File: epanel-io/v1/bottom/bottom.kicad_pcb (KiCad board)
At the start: 2 copper layers, 86.5 x 103 mm, 152 parts, among them J1 Conn_01x05_Male, J2 Screw_Terminal_01x05, J3 Screw_Terminal_01x05, J4 Screw_Terminal_01x05, J5 Screw_Terminal_01x05, J6 Screw_Terminal_01x03, J7 Screw_Terminal_01x03, Q1 IRF830, Q10 IRF830, Q11 IRF830, Q12 IRF830, Q13 IRF830, Q14 IRF830, Q15 IRF830, Q16 IRF830, Q17 IRF830, Q18 IRF830, Q19 IRF830, Q2 IRF830, Q20 IRF830, Q3 IRF830, Q4 IRF830, Q5 IRF830, Q6 IRF830, Q7 IRF830, Q8 IRF830, Q9 IRF830, U1 Pico, U10 4N35, U11 H11AA1, U12 4N35, U13 H11AA1, U14 4N35, U15 H11AA1, U16 4N35, U17 H11AA1, U18 4N35, U19 H11AA1, U2 H11AA1, U20 4N35, U21 H11AA1, U22 4N35, U3 H11AA1, U4 4N35, U5 H11AA1, U6 4N35, U7 H11AA1, U8 4N35, U9 H11AA1

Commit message: bottom board first draft
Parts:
- removed C1, C10, C2, C3, C4, C5, C6, C7, C8, C9: 2.2uF/63V, Capacitor_SMD:C_1206_3216Metric
- removed D1, D11, D13, D15, D17, D19, D3, D5, D7, D9: 10V/0.4W, Diode_SMD:D_SOD-123
- removed D10, D12, D14, D16, D18, D2, D20, D4, D6, D8: 1N4007, Diode_SMD:D_SMA
- removed R1, R11, R18, R25, R32, R39, R4, R46, R53, R60, R67: 10KΩ, Resistor_SMD:R_0603_1608Metric
- removed R10, R12, R13, R16, R17, R19, R2, R20, R23, R24, R26, R27, R3, R30, R31, R33, R34, R37, R38, R40, R41, R44, R45, R47, R48, R5, R51, R52, R54, R55, R58, R59, R6, R61, R62, R65, R66, R68, R69, R72, R73, R9: 33KΩ/0.5W, Resistor_SMD:R_0805_2012Metric
- removed R14, R21, R28, R35, R42, R49, R56, R63, R7, R70: 330Ω, Resistor_SMD:R_0603_1608Metric
- removed R15, R22, R29, R36, R43, R50, R57, R64, R71, R8: 22KΩ, Resistor_SMD:R_0603_1608Metric
- removed U1: Pico, MCU_RaspberryPi_and_Boards:RPi_Pico_SMD_TH
- removed U10, U12, U14, U16, U18, U20, U22, U4, U6, U8: 4N35, Package_DIP:SMDIP-6_W7.62mm
- removed U11, U13, U15, U17, U19, U2, U21, U3, U5, U7, U9: H11AA1, Package_DIP:SMDIP-6_W9.53mm
- added J10: Conn_01x04_Male, Connector_PinHeader_2.54mm:PinHeader_1x04_P2.54mm_Vertical, F.Cu at (173.4, 107.9)
- added J11: Screw_Terminal_01x03, TerminalBlock:TerminalBlock_bornier-3_P5.08mm, F.Cu at (104.1, 82.5)
- added J12: Screw_Terminal_01x03, TerminalBlock:TerminalBlock_bornier-3_P5.08mm, F.Cu at (182.2, 82.5)
- added J13: Conn_01x05_Male, Connector_PinHeader_2.54mm:PinHeader_1x05_P2.54mm_Vertical, F.Cu at (113.0, 110.5)
- added J14: Conn_01x05_Male, Connector_PinHeader_2.54mm:PinHeader_1x05_P2.54mm_Vertical, F.Cu at (102.7, 110.5)
- added J15: Conn_01x05_Male, Connector_PinHeader_2.54mm:PinHeader_1x05_P2.54mm_Vertical, F.Cu at (107.3, 110.5)
- added J8: Screw_Terminal_01x05, TerminalBlock:TerminalBlock_bornier-5_P5.08mm, F.Cu at (182.2, 127.6)
- added J9: Conn_01x04_Male, Connector_PinHeader_2.54mm:PinHeader_1x04_P2.54mm_Vertical, F.Cu at (113.0, 83.8)
- J2: value Screw_Terminal_01x05 -> Conn_01x08_Male; footprint TerminalBlock:TerminalBlock_bornier-5_P5.08mm -> Connector_PinHeader_2.54mm:PinHeader_1x08_P2.54mm_Vertical
- J5: value Screw_Terminal_01x05 -> Conn_01x05_Male; footprint TerminalBlock:TerminalBlock_bornier-5_P5.08mm -> Connector_PinHeader_2.54mm:PinHeader_1x05_P2.54mm_Vertical
- J6: value Screw_Terminal_01x03 -> Conn_01x08_Male; footprint TerminalBlock:TerminalBlock_bornier-3_P5.08mm -> Connector_PinHeader_2.54mm:PinHeader_1x08_P2.54mm_Vertical
- J7: value Screw_Terminal_01x03 -> Screw_Terminal_01x05; footprint TerminalBlock:TerminalBlock_bornier-3_P5.08mm -> TerminalBlock:TerminalBlock_bornier-5_P5.08mm
- moved Q19 246.6 mm to (136.8, 101.7), turned to 90 degrees
- moved Q20 229.5 mm to (123.0, 101.7), turned to 90 degrees
- moved Q18 224.5 mm to (164.7, 101.7), turned to 90 degrees
- moved Q17 216.1 mm to (150.9, 101.7), turned to 90 degrees
- moved J3 107.8 mm to (104.1, 127.6)
- moved J4 106.5 mm to (182.2, 55.2)
- moved J5 96.5 mm to (113.0, 60.3), turned to 0 degrees
- moved J6 87.4 mm to (173.4, 134.6), turned to 180 degrees
- moved J7 82.1 mm to (104.1, 55.2)
- moved J2 71.8 mm to (173.4, 72.4), turned to 0 degrees
- moved Q3 33.5 mm to (150.9, 59.1), turned to 90 degrees
- moved Q6 32.4 mm to (136.8, 76.3), turned to 90 degrees
- moved Q4 25.6 mm to (150.9, 76.3), turned to 90 degrees
- moved J1 25.0 mm to (113.0, 132.7)
- moved Q5 20.7 mm to (136.8, 59.1), turned to 90 degrees
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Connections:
- J1 pad 1: +5V -> Net-(J1-Pad1)
- J1 pad 2: GND -> Net-(J1-Pad2)
- J2 pad 1: /Input 1/NEUT -> Net-(J2-Pad1)
- J2 pad 2: /Input 1/INPUT -> Net-(J2-Pad2)
- J2 pad 3: /Input 2/INPUT -> Net-(J2-Pad3)
- J2 pad 4: /Input 3/INPUT -> Net-(J2-Pad4)
- J2 pad 5: /Input 4/INPUT -> Net-(J2-Pad5)
- J3 pad 1: /Output 1/LINE -> Net-(J1-Pad1)
- J3 pad 2: /Output 1/OUTPUT -> Net-(J1-Pad2)
- J3 pad 3: /Output 2/OUTPUT -> Net-(J1-Pad3)
- J3 pad 4: /Output 3/OUTPUT -> Net-(J1-Pad4)
- J3 pad 5: /Output 4/OUTPUT -> Net-(J1-Pad5)
- J4 pad 1: /Input 5/NEUT -> Net-(J4-Pad1)
- J4 pad 2: /Input 5/INPUT -> Net-(J4-Pad2)
- J4 pad 3: /Input 6/INPUT -> Net-(J4-Pad3)
- J4 pad 4: /Input 7/INPUT -> Net-(J4-Pad4)
- J4 pad 5: /Input 8/INPUT -> Net-(J4-Pad5)
- J5 pad 1: /Output 5/LINE -> Net-(J5-Pad1)
- J5 pad 2: /Output 5/OUTPUT -> Net-(J5-Pad2)
- J5 pad 3: /Output 7/OUTPUT -> Net-(J5-Pad3)
- J5 pad 4: /Output 6/OUTPUT -> Net-(J5-Pad4)
- J5 pad 5: /Output 8/OUTPUT -> Net-(J5-Pad5)
- J6 pad 1: /Input 10/NEUT -> Net-(J6-Pad1)
- J6 pad 2: /Input 9/INPUT -> Net-(J6-Pad2)
- J6 pad 3: /Input 10/INPUT -> Net-(J6-Pad3)
- J7 pad 1: /Output 10/LINE -> Net-(J5-Pad1)
- J7 pad 2: /Output 9/OUTPUT -> Net-(J5-Pad2)
- J7 pad 3: /Output 10/OUTPUT -> Net-(J5-Pad3)
- Q1 pad 1: Net-(Q1-Pad1) -> Net-(J2-Pad2)
- Q1 pad 2: /Output 1/LINE -> Net-(J4-Pad1)
- Q1 pad 3: Net-(C1-Pad2) -> Net-(J2-Pad1)
- Q10 pad 1: Net-(Q10-Pad1) -> Net-(J6-Pad2)
- Q10 pad 2: /Output 5/OUTPUT -> Net-(J8-Pad2)
- Q10 pad 3: Net-(C5-Pad2) -> Net-(J6-Pad1)
- Q11 pad 1: Net-(Q11-Pad1) -> Net-(J6-Pad4)
- Q11 pad 2: /Output 5/LINE -> Net-(J8-Pad1)
- Q11 pad 3: Net-(C6-Pad2) -> Net-(J6-Pad3)
- Q12 pad 1: Net-(Q11-Pad1) -> Net-(J6-Pad4)
- Q12 pad 2: /Output 7/OUTPUT -> Net-(J8-Pad3)
- Q12 pad 3: Net-(C6-Pad2) -> Net-(J6-Pad3)
- Q13 pad 1: Net-(Q13-Pad1) -> Net-(J6-Pad6)
- Q13 pad 2: /Output 5/LINE -> Net-(J8-Pad1)
- Q13 pad 3: Net-(C7-Pad2) -> Net-(J6-Pad5)
- Q14 pad 1: Net-(Q13-Pad1) -> Net-(J6-Pad6)
- Q14 pad 2: /Output 6/OUTPUT -> Net-(J8-Pad4)
- Q14 pad 3: Net-(C7-Pad2) -> Net-(J6-Pad5)
- Q15 pad 1: Net-(Q15-Pad1) -> Net-(J6-Pad8)
- Q15 pad 2: /Output 5/LINE -> Net-(J8-Pad1)
- Q15 pad 3: Net-(C8-Pad2) -> Net-(J6-Pad7)
- Q16 pad 1: Net-(Q15-Pad1) -> Net-(J6-Pad8)
- Q16 pad 2: /Output 8/OUTPUT -> Net-(J8-Pad5)
- Q16 pad 3: Net-(C8-Pad2) -> Net-(J6-Pad7)
- Q17 pad 2: /Output 10/LINE -> Net-(J12-Pad1)
- Q18 pad 2: /Output 9/OUTPUT -> Net-(J12-Pad2)
- Q19 pad 2: /Output 10/LINE -> Net-(J12-Pad1)
- Q2 pad 1: Net-(Q1-Pad1) -> Net-(J2-Pad2)
- Q2 pad 2: /Output 1/OUTPUT -> Net-(J4-Pad2)
- Q2 pad 3: Net-(C1-Pad2) -> Net-(J2-Pad1)
- Q20 pad 2: /Output 10/OUTPUT -> Net-(J12-Pad3)
- Q3 pad 1: Net-(Q3-Pad1) -> Net-(J2-Pad4)
- Q3 pad 2: /Output 1/LINE -> Net-(J4-Pad1)
- Q3 pad 3: Net-(C2-Pad2) -> Net-(J2-Pad3)
- Q4 pad 1: Net-(Q3-Pad1) -> Net-(J2-Pad4)
- Q4 pad 2: /Output 2/OUTPUT -> Net-(J4-Pad3)
- Q4 pad 3: Net-(C2-Pad2) -> Net-(J2-Pad3)
- Q5 pad 1: Net-(Q5-Pad1) -> Net-(J2-Pad6)
- Q5 pad 2: /Output 1/LINE -> Net-(J4-Pad1)
- Q5 pad 3: Net-(C3-Pad2) -> Net-(J2-Pad5)
- Q6 pad 1: Net-(Q5-Pad1) -> Net-(J2-Pad6)
- Q6 pad 2: /Output 3/OUTPUT -> Net-(J4-Pad4)
- Q6 pad 3: Net-(C3-Pad2) -> Net-(J2-Pad5)
- Q7 pad 1: Net-(Q7-Pad1) -> Net-(J2-Pad8)
- Q7 pad 2: /Output 1/LINE -> Net-(J4-Pad1)
- Q7 pad 3: Net-(C4-Pad2) -> Net-(J2-Pad7)
- Q8 pad 1: Net-(Q7-Pad1) -> Net-(J2-Pad8)
- Q8 pad 2: /Output 4/OUTPUT -> Net-(J4-Pad5)
- Q8 pad 3: Net-(C4-Pad2) -> Net-(J2-Pad7)
- Q9 pad 1: Net-(Q10-Pad1) -> Net-(J6-Pad2)
- Q9 pad 2: /Output 5/LINE -> Net-(J8-Pad1)
- Q9 pad 3: Net-(C5-Pad2) -> Net-(J6-Pad1)
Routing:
- net /Output 1/LINE: track 161.2 -> 0.00 mm, vias 2 -> 0
- net Net-(J8-Pad1): track 0.00 -> 113.0 mm
- net /Input 1/NEUT: track 109.6 -> 0.00 mm, vias 4 -> 0
- net Net-(J12-Pad1): track 0.00 -> 108.3 mm, vias 0 -> 1
- net /Output 5/LINE: track 97.6 -> 0.00 mm
- net Net-(J4-Pad1): track 0.00 -> 96.1 mm
- net Net-(J4-Pad5): track 0.00 -> 90.0 mm, vias 0 -> 1
- net Net-(J8-Pad5): track 0.00 -> 87.8 mm, vias 0 -> 1
- net /Output 8/OUTPUT: track 87.8 -> 0.00 mm, vias 1 -> 0
- net Net-(J6-Pad8): track 0.00 -> 83.9 mm, vias 0 -> 1
- net Net-(J2-Pad8): track 0.00 -> 79.3 mm
- net Net-(J12-Pad3): track 0.00 -> 75.2 mm, vias 0 -> 1
- net Net-(J6-Pad7): track 0.00 -> 73.3 mm, vias 0 -> 1
- net Net-(J2-Pad7): track 0.00 -> 72.8 mm
- net Net-(J4-Pad4): track 0.00 -> 71.7 mm, vias 0 -> 1
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
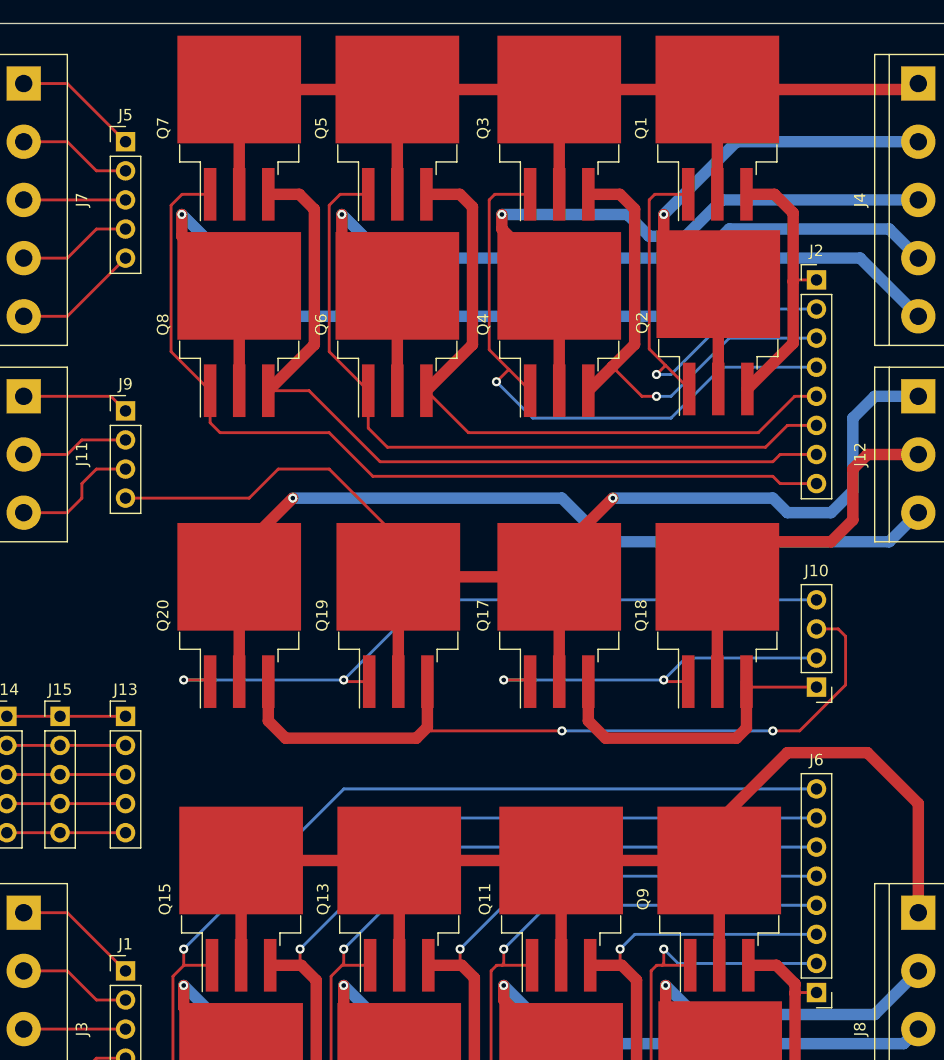
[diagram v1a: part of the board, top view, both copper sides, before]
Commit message: add labels
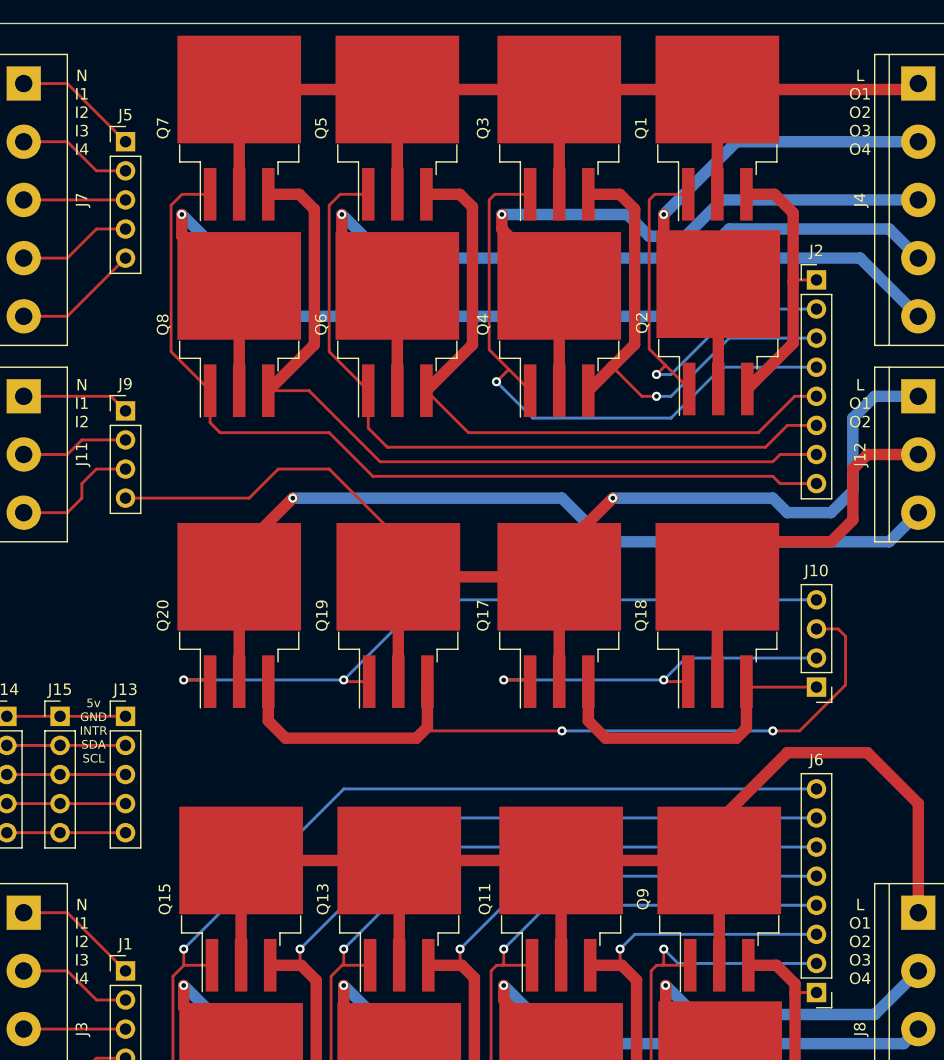
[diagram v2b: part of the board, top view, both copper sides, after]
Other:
- board text added: "5v GND INTR SDA SCL"
- board text added: "L O1 O2"
- board text added: "L O1 O2 O3 O4"
- board text added: "N I1 I2"
- board text added: "N I1 I2 I3 I4"
